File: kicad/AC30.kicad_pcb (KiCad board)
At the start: 2 copper layers, 173 x 97.5 mm, 84 parts, among them IC10 555, IC11 4001, IC12 1489, IC13 4070, IC14 4053, IC15 1488, IC6 4053, IC7 4049, IC8 4013, IC9 4023, J1 Front panel harness 1, J2 Front panel harness 2, J3 Computer interface (COMP), J4 Control interface, J5 Terminal interface (TERM), Q10 2N5087, Q11 2N5087, Q5 2N5210, Q6 2N5210, Q7 2N5210, Q8 2N5210, Q9 2N5087

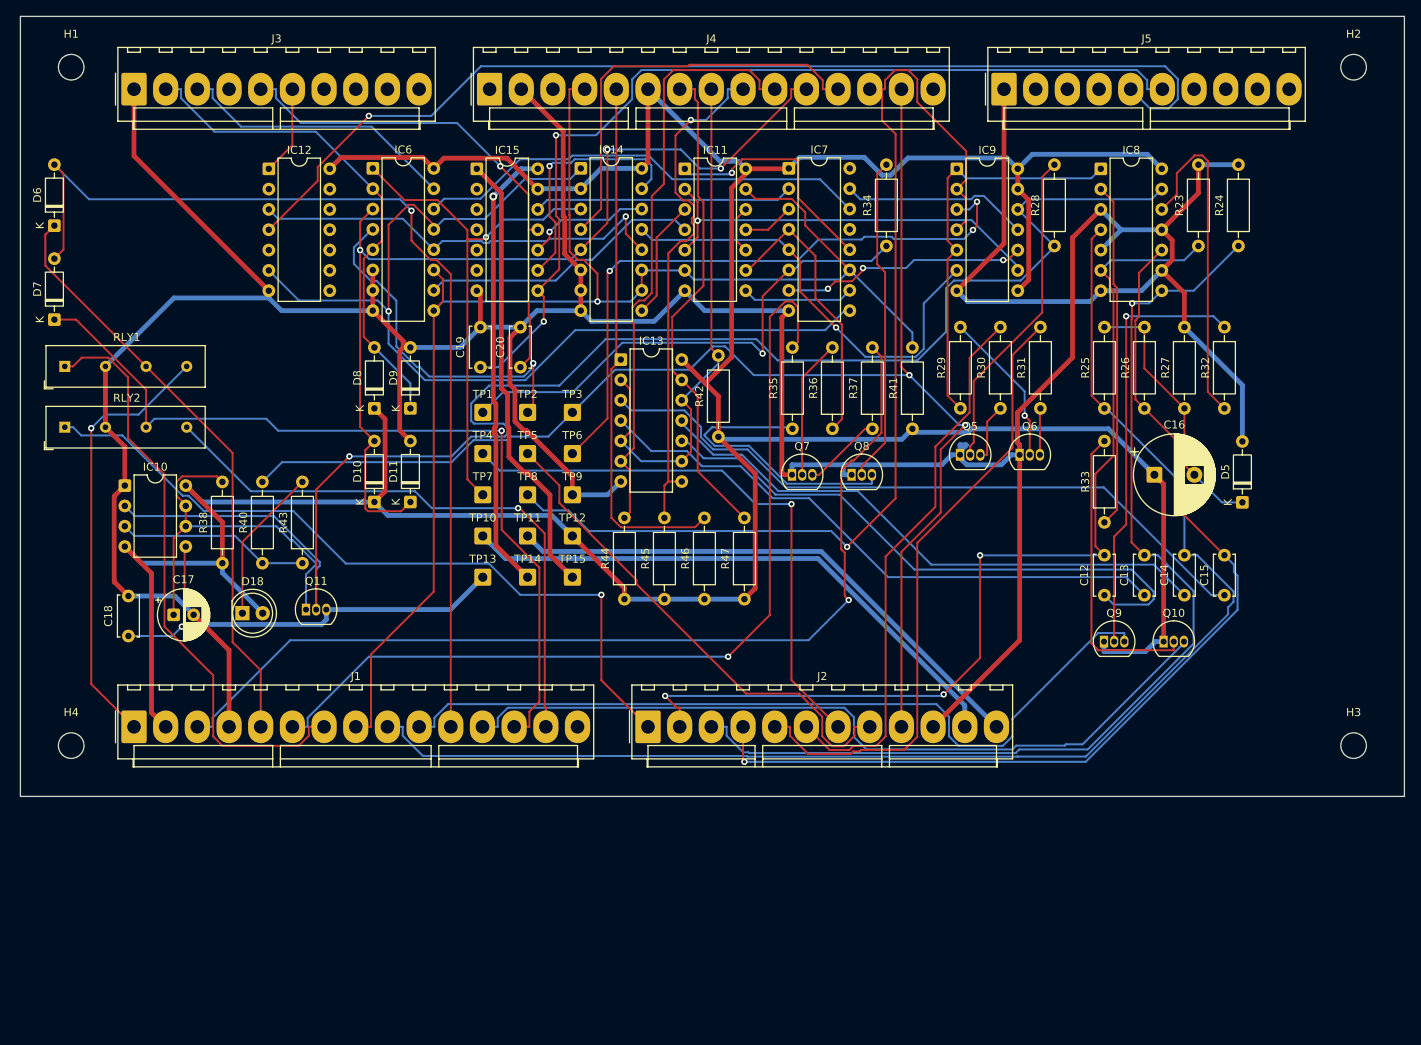
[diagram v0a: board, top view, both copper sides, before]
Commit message: Wire mod/demod and external power supply; retry routing until DRC-clean
- Transcribe docs/ac30_mod_demod.pdf onto sheet 2: modulator (IC5A/B,
  IC2A, IC4A filter) and demodulator (IC4B comparator, IC3C/D edge pulses,
  carrier detect, missing-pulse detector, R16 timer, IC1A data out, 16X
  clock out). The mod/demod interface solder pads are removed.
- Transcribe docs/ac30_PS.pdf onto new sheet 3 as an external unit (no
  footprints): line cord, S6, F1, T1, bridge D14-D17, +/-13 V, +/-7.5 V
  zener rails, 7805. IC16 GND taken as GND (drawing ties it to -13 V).
- Board gets through-hole power input pads TP1-TP6 (+5V, GND, +13V, -13V,
  +7.5V, -7.5V) with rail names on the silkscreen, plus C23-C25 +5 V
  bypass. IC4 on +/-7.5 V, IC15 on +/-13 V. J2 18 VAC pins now unused.
- Corner mounting holes H1-H4, 6.35 mm in from each edge (artwork).
- Placement weighs all nets except +5V/GND; build.sh routes the placed
  board afresh up to 4 times and keeps the first DRC-clean result.
- Board 173.0 x 121.5 mm, fully routed; ERC, DRC (all severities) and
  schematic parity clean. AC30-settings.md updated.

Co-Authored-By: Claude Opus 5.5 <noreply@anthropic.com>
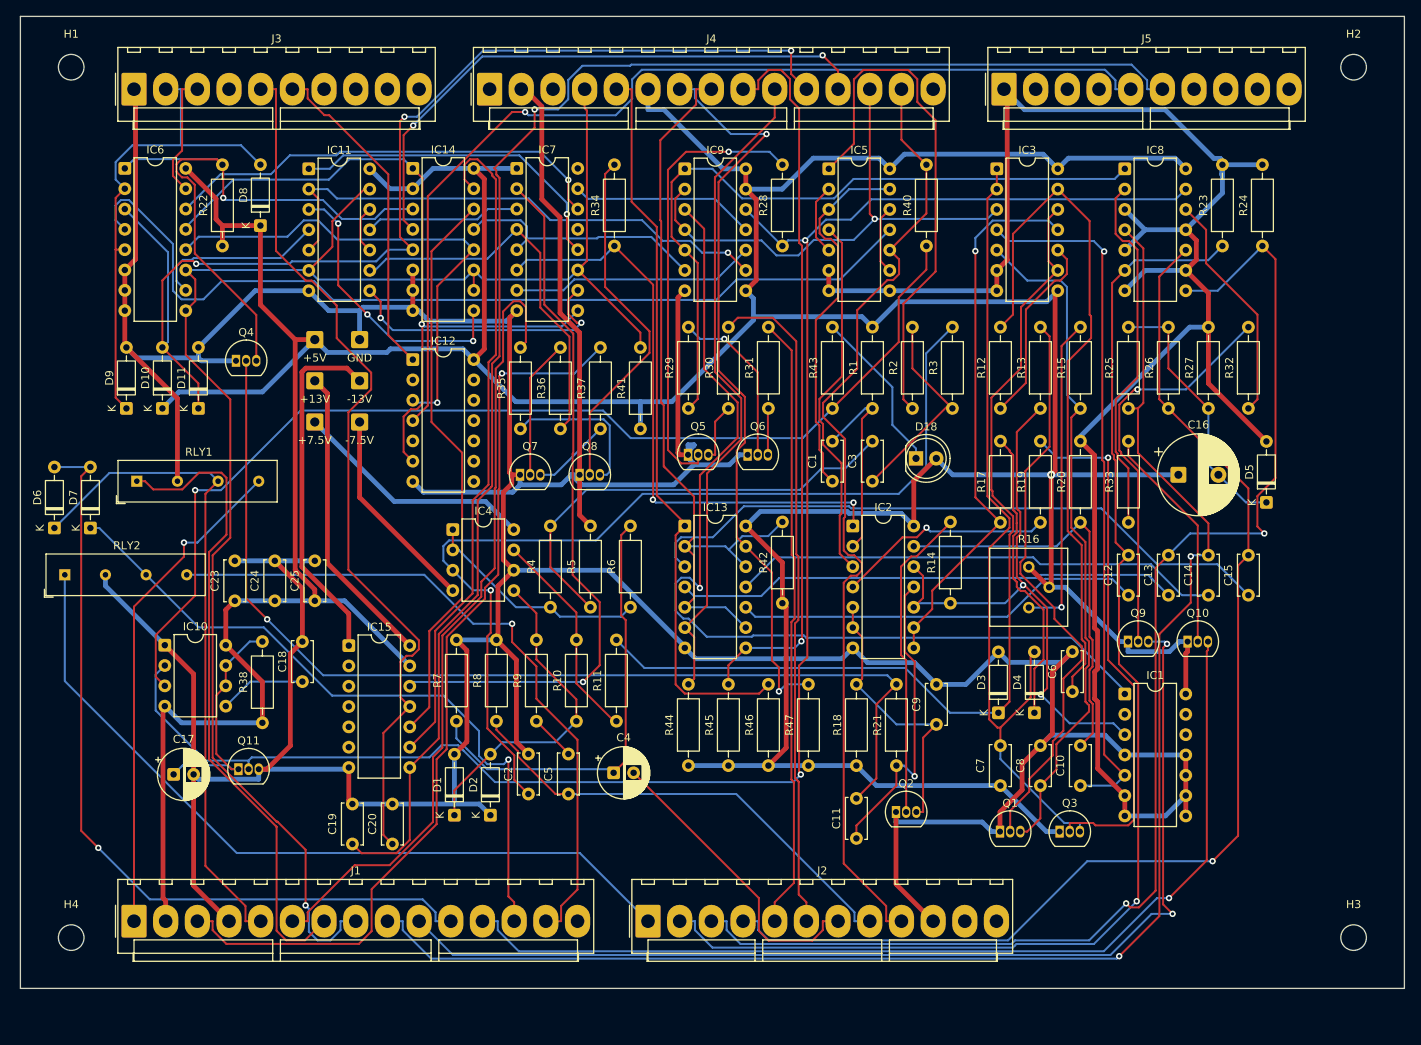
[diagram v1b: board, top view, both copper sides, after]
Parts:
- removed TP10: 18 VAC A (from J2 / T1), Connector_Wire:SolderWire-0.5sqmm_1x01_D0.9mm_OD2.1mm
- removed TP11: 18 VAC B (from J2 / T1), Connector_Wire:SolderWire-0.5sqmm_1x01_D0.9mm_OD2.1mm
- removed TP12: +5V (regulated), Connector_Wire:SolderWire-0.5sqmm_1x01_D0.9mm_OD2.1mm
- removed TP13: GND (power), Connector_Wire:SolderWire-0.5sqmm_1x01_D0.9mm_OD2.1mm
- removed TP14: RS-232 V+ (IC15 pin 14), Connector_Wire:SolderWire-0.5sqmm_1x01_D0.9mm_OD2.1mm
- removed TP15: RS-232 V- (IC15 pin 1), Connector_Wire:SolderWire-0.5sqmm_1x01_D0.9mm_OD2.1mm
- removed TP7: 16X CLOCK OUT (from demodulator), Connector_Wire:SolderWire-0.5sqmm_1x01_D0.9mm_OD2.1mm
- removed TP8: CARRIER DETECT (from demodulator), Connector_Wire:SolderWire-0.5sqmm_1x01_D0.9mm_OD2.1mm
- removed TP9: GND (mod/demod), Connector_Wire:SolderWire-0.5sqmm_1x01_D0.9mm_OD2.1mm
- added C1: 1000pF, Capacitor_THT:C_Disc_D5.0mm_W2.5mm_P5.00mm, F.Cu at (131.5, 87.6)
- added C10: 2700pF, Capacitor_THT:C_Disc_D5.0mm_W2.5mm_P5.00mm, F.Cu at (162.5, 125.7)
- added C11: 470pF, Capacitor_THT:C_Disc_D5.0mm_W2.5mm_P5.00mm, F.Cu at (134.5, 132.2)
- added C2: 2000pF, Capacitor_THT:C_Disc_D5.0mm_W2.5mm_P5.00mm, F.Cu at (93.5, 126.7)
- added C23: 0.1uF, Capacitor_THT:C_Disc_D5.0mm_W2.5mm_P5.00mm, F.Cu at (56.8, 102.5)
- added C24: 0.1uF, Capacitor_THT:C_Disc_D5.0mm_W2.5mm_P5.00mm, F.Cu at (61.8, 102.5)
- added C25: 0.1uF, Capacitor_THT:C_Disc_D5.0mm_W2.5mm_P5.00mm, F.Cu at (66.8, 102.5)
- added C3: 0.022uF, Capacitor_THT:C_Disc_D5.0mm_W2.5mm_P5.00mm, F.Cu at (136.5, 87.6)
- added C4: 1uF 15V, Capacitor_THT:CP_Radial_D6.3mm_P2.50mm, F.Cu at (104.2, 124.0)
- added C5: 0.01uF, Capacitor_THT:C_Disc_D5.0mm_W2.5mm_P5.00mm, F.Cu at (98.5, 126.7)
- added C6: 1000pF, Capacitor_THT:C_Disc_D5.0mm_W2.5mm_P5.00mm, F.Cu at (161.5, 113.9)
- added C7: 0.047uF, Capacitor_THT:C_Disc_D5.0mm_W2.5mm_P5.00mm, F.Cu at (152.5, 125.7)
- added C8: 0.022uF, Capacitor_THT:C_Disc_D5.0mm_W2.5mm_P5.00mm, F.Cu at (157.5, 125.7)
- added C9: 0.047uF, Capacitor_THT:C_Disc_D5.0mm_W2.5mm_P5.00mm, F.Cu at (144.5, 118.0)
- added D1: 1N4148, Diode_THT:D_DO-35_SOD27_P7.62mm_Horizontal, F.Cu at (84.2, 129.3)
- added D2: 1N4148, Diode_THT:D_DO-35_SOD27_P7.62mm_Horizontal, F.Cu at (88.8, 129.3)
- added D3: 1N4732 4.7V, Diode_THT:D_DO-35_SOD27_P7.62mm_Horizontal, F.Cu at (152.2, 116.5)
- added D4: 1N4148, Diode_THT:D_DO-35_SOD27_P7.62mm_Horizontal, F.Cu at (156.8, 116.5)
- added IC1: 4013, Package_DIP:DIP-14_W7.62mm, F.Cu at (168.1, 114.2)
- added IC2: 4001, Package_DIP:DIP-14_W7.62mm, F.Cu at (134.1, 93.2)
- added IC3: 4070, Package_DIP:DIP-14_W7.62mm, F.Cu at (152.1, 48.5)
- added IC4: 4558, Package_DIP:DIP-8_W7.62mm, F.Cu at (84.0, 93.7)
- added IC5: 4013, Package_DIP:DIP-14_W7.62mm, F.Cu at (131.1, 48.5)
- added Q1: 2N5210, Package_TO_SOT_THT:TO-92_Inline, F.Cu at (152.4, 131.4)
- added Q2: 2N5210, Package_TO_SOT_THT:TO-92_Inline, F.Cu at (139.4, 128.9)
- added Q3: 2N5087, Package_TO_SOT_THT:TO-92_Inline, F.Cu at (159.9, 131.4)
- added Q4: 2N5210, Package_TO_SOT_THT:TO-92_Inline, F.Cu at (57.0, 72.5)
- added R1: 33K, Resistor_THT:R_Axial_DIN0207_L6.3mm_D2.5mm_P10.16mm_Horizontal, F.Cu at (136.5, 78.5)
- added R10: 330K, Resistor_THT:R_Axial_DIN0207_L6.3mm_D2.5mm_P10.16mm_Horizontal, F.Cu at (99.5, 117.6)
- added R11: 10K, Resistor_THT:R_Axial_DIN0207_L6.3mm_D2.5mm_P10.16mm_Horizontal, F.Cu at (104.5, 117.6)
- added R12: 10K, Resistor_THT:R_Axial_DIN0207_L6.3mm_D2.5mm_P10.16mm_Horizontal, F.Cu at (152.5, 78.5)
- added R13: 22K, Resistor_THT:R_Axial_DIN0207_L6.3mm_D2.5mm_P10.16mm_Horizontal, F.Cu at (157.5, 78.5)
- added R14: 22K, Resistor_THT:R_Axial_DIN0207_L6.3mm_D2.5mm_P10.16mm_Horizontal, F.Cu at (146.2, 102.8)
- added R15: 10K, Resistor_THT:R_Axial_DIN0207_L6.3mm_D2.5mm_P10.16mm_Horizontal, F.Cu at (162.5, 78.5)
- added R16: 20K trim, Potentiometer_THT:Potentiometer_Bourns_3386P_Vertical, F.Cu at (156.1, 103.4)
- added R17: 100K, Resistor_THT:R_Axial_DIN0207_L6.3mm_D2.5mm_P10.16mm_Horizontal, F.Cu at (152.5, 92.8)
- added R18: 100K, Resistor_THT:R_Axial_DIN0207_L6.3mm_D2.5mm_P10.16mm_Horizontal, F.Cu at (134.5, 123.2)
- added R19: 10K, Resistor_THT:R_Axial_DIN0207_L6.3mm_D2.5mm_P10.16mm_Horizontal, F.Cu at (157.5, 92.8)
- added R2: 10K, Resistor_THT:R_Axial_DIN0207_L6.3mm_D2.5mm_P10.16mm_Horizontal, F.Cu at (141.5, 78.5)
- added R20: 10K, Resistor_THT:R_Axial_DIN0207_L6.3mm_D2.5mm_P10.16mm_Horizontal, F.Cu at (162.5, 92.8)
- added R21: 10K, Resistor_THT:R_Axial_DIN0207_L6.3mm_D2.5mm_P10.16mm_Horizontal, F.Cu at (139.5, 123.2)
- added R22: 10K, Resistor_THT:R_Axial_DIN0207_L6.3mm_D2.5mm_P10.16mm_Horizontal, F.Cu at (55.2, 58.2)
- added R3: 10K, Resistor_THT:R_Axial_DIN0207_L6.3mm_D2.5mm_P10.16mm_Horizontal, F.Cu at (146.5, 78.5)
- added R4: 330, Resistor_THT:R_Axial_DIN0207_L6.3mm_D2.5mm_P10.16mm_Horizontal, F.Cu at (96.2, 103.3)
- added R5: 2.2K, Resistor_THT:R_Axial_DIN0207_L6.3mm_D2.5mm_P10.16mm_Horizontal, F.Cu at (101.2, 103.3)
- added R6: 4.7K, Resistor_THT:R_Axial_DIN0207_L6.3mm_D2.5mm_P10.16mm_Horizontal, F.Cu at (106.2, 103.3)
- added R7: 470, Resistor_THT:R_Axial_DIN0207_L6.3mm_D2.5mm_P10.16mm_Horizontal, F.Cu at (84.5, 117.6)
- added R8: 100K, Resistor_THT:R_Axial_DIN0207_L6.3mm_D2.5mm_P10.16mm_Horizontal, F.Cu at (89.5, 117.6)
- added R9: 10K, Resistor_THT:R_Axial_DIN0207_L6.3mm_D2.5mm_P10.16mm_Horizontal, F.Cu at (94.5, 117.6)
- TP1: value DATA IN (to modulator) -> +5V
- TP2: value 16X CLOCK IN (to modulator) -> GND
- TP3: value ~{CARRIER ENABLE} (to modulator) -> +13V
- TP4: value AUDIO OUT (from modulator) -> -13V
- TP5: value AUDIO IN (to demodulator) -> +7.5V
- TP6: value DATA OUT (from demodulator) -> -7.5V
- moved R40 92.0 mm to (143.2, 58.2)
- moved D18 86.4 mm to (141.9, 84.8)
- moved R43 69.0 mm to (131.5, 78.5)
- moved C19 61.7 mm to (71.5, 132.9)
- moved C20 61.7 mm to (76.5, 132.9)
- moved IC15 61.7 mm to (71.0, 108.2)
- moved IC11 47.0 mm to (66.0, 48.5)
- moved D6 37.8 mm to (34.2, 93.5)
- moved D9 35.5 mm to (43.2, 78.5)
- moved IC9 34.0 mm to (113.0, 48.5)
- moved IC7 34.0 mm to (92.0, 48.5)
- moved Q6 34.0 mm to (120.9, 84.3)
- moved Q7 34.0 mm to (92.5, 86.8)
- moved Q8 34.0 mm to (99.9, 86.8)
- moved R28 34.0 mm to (125.2, 58.2)
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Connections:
- IC15 pad 1: V_RS232- -> -13V
- IC15 pad 14: V_RS232+ -> +13V
- J2 pad 11: 18VAC_A -> unconnected-(J2-Pin_11-Pad11)
- J2 pad 12: 18VAC_B -> unconnected-(J2-Pin_12-Pad12)
- TP1 pad 1: DATA_IN -> +5V
- TP2 pad 1: CLOCK_IN -> GND
- TP3 pad 1: CARRIER_EN_N -> +13V
- TP4 pad 1: AUDIO_OUT -> -13V
- TP5 pad 1: AUDIO_IN -> +7.5V
- TP6 pad 1: DATA_OUT -> -7.5V
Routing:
- net GND: track 557.8 -> 869.7 mm
- net +5V: track 441.4 -> 639.8 mm, vias 0 -> 1
- net /Mod/Demod & power input/DEM_Q4B: track 0.00 -> 131.8 mm, vias 0 -> 1
- net /Mod/Demod & power input/DEM_LIM: track 0.00 -> 120.7 mm
- net /Mod/Demod & power input/MOD_F2: track 0.00 -> 120.3 mm, vias 0 -> 1
- net /DELAY_OUT: track 24.1 -> 138.9 mm, vias 0 -> 1
- net /Mod/Demod & power input/DEM_CD: track 0.00 -> 102.8 mm
- net /Mod/Demod & power input/DEM_DLY: track 0.00 -> 87.6 mm
- net /Mod/Demod & power input/DEM_BIT: track 0.00 -> 87.4 mm, vias 0 -> 1
- net /Mod/Demod & power input/DEM_TIMER: track 0.00 -> 85.3 mm
- net /TERM_RS232_IN: track 117.4 -> 190.8 mm, vias 2 -> 1
- net /Mod/Demod & power input/DEM_PULSE: track 0.00 -> 72.8 mm, vias 0 -> 2
- net /Mod/Demod & power input/DEM_Q1B: track 0.00 -> 71.9 mm
- net 18VAC_A: track 71.7 -> 0.00 mm
- net CLOCK_IN: track 44.6 -> 114.6 mm, vias 1 -> 0
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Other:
- board size 173 x 97.5 mm -> 173 x 121.5 mm

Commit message: Replace power input pads with J12, a 6-pin KK-396 header on the bottom edge
- J12 (Molex KK-396 A-41791-0006) replaces solder pads TP1-TP6 for the
  external supply: 1 GND, 2 +5V, 3 +13V, 4 -13V, 5 +7.5V, 6 -7.5V.
  Placed in the bottom connector row next to J2, clear of the corner hole.
- build.sh: if no routing attempt is DRC-clean, up to 3 finishing passes
  route only what is left on the best result, each checked by DRC.
- Board 173.5 x 122.0 mm, fully routed; ERC, DRC (all severities) and
  schematic parity clean. AC30-settings.md updated (power input, drill
  table, routing, positions).

Co-Authored-By: Claude Opus 5.5 <noreply@anthropic.com>
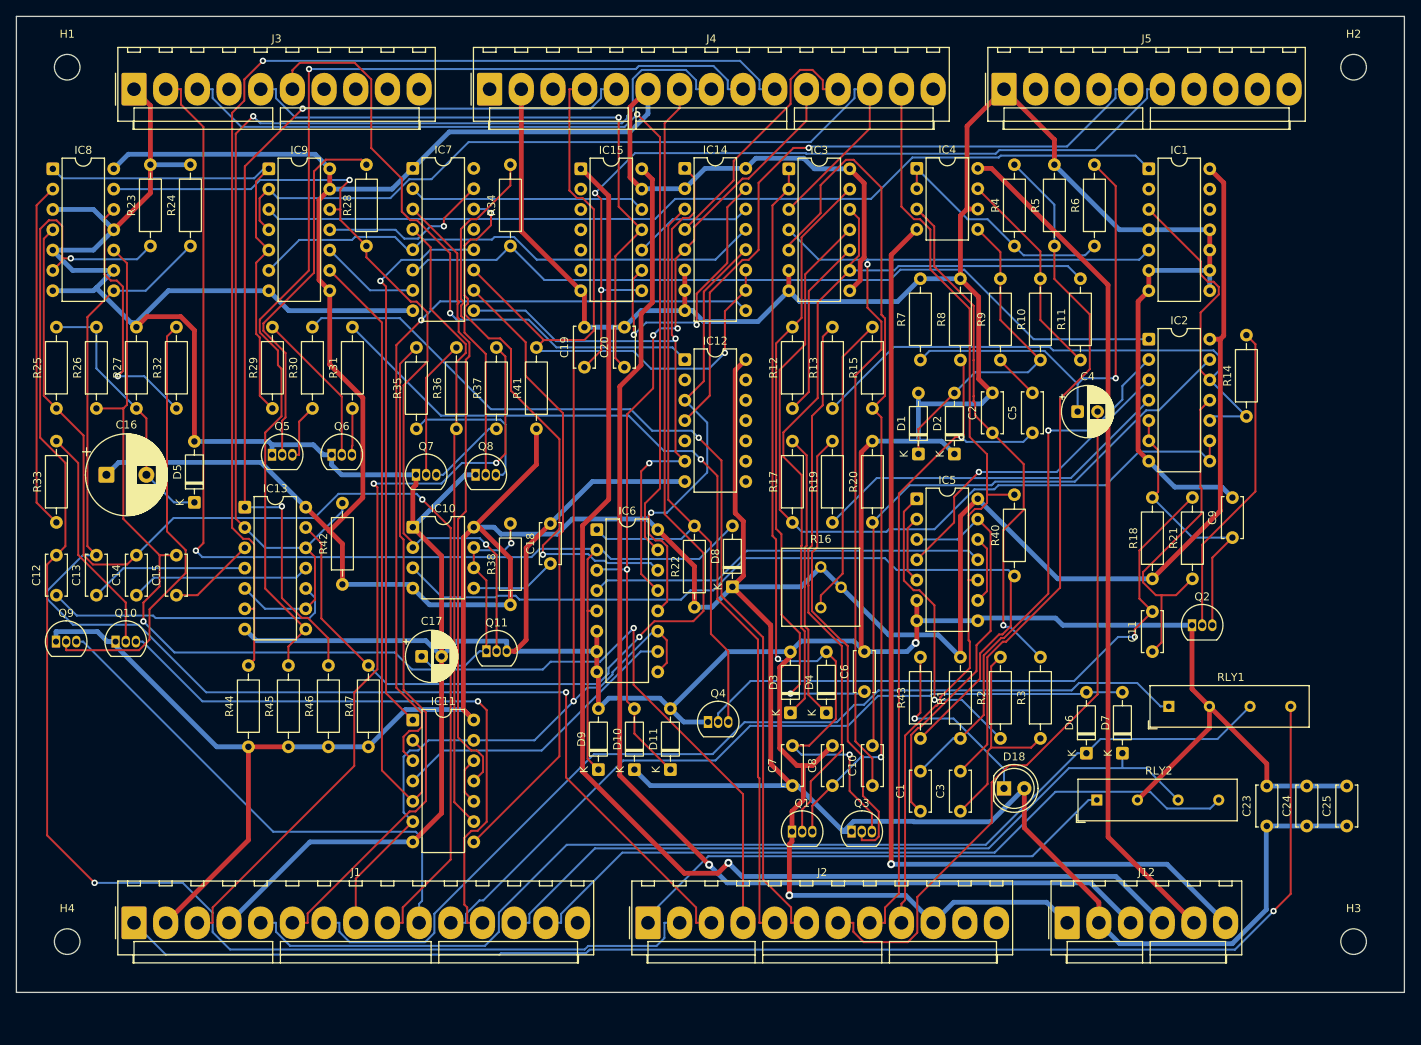
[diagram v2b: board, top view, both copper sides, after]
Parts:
- removed TP1: +5V, Connector_Wire:SolderWire-0.5sqmm_1x01_D0.9mm_OD2.1mm
- removed TP2: GND, Connector_Wire:SolderWire-0.5sqmm_1x01_D0.9mm_OD2.1mm
- removed TP3: +13V, Connector_Wire:SolderWire-0.5sqmm_1x01_D0.9mm_OD2.1mm
- removed TP4: -13V, Connector_Wire:SolderWire-0.5sqmm_1x01_D0.9mm_OD2.1mm
- removed TP5: +7.5V, Connector_Wire:SolderWire-0.5sqmm_1x01_D0.9mm_OD2.1mm
- removed TP6: -7.5V, Connector_Wire:SolderWire-0.5sqmm_1x01_D0.9mm_OD2.1mm
- added J12: Power input, Connector_Molex:Molex_KK-396_A-41791-0006_1x06_P3.96mm_Vertical, F.Cu at (160.8, 142.8)
- moved C12 134.0 mm to (34.5, 101.8)
- moved C13 134.0 mm to (39.5, 101.8)
- moved C14 134.0 mm to (44.5, 101.8)
- moved C15 134.0 mm to (49.5, 101.8)
- moved C16 134.0 mm to (40.8, 86.8)
- moved D5 134.0 mm to (51.8, 90.2)
- moved IC8 134.0 mm to (34.0, 48.5)
- moved Q10 134.0 mm to (41.9, 107.7)
- moved Q9 134.0 mm to (34.5, 107.7)
- moved R23 134.0 mm to (46.2, 58.2)
- moved R24 134.0 mm to (51.2, 58.2)
- moved R25 134.0 mm to (34.5, 78.5)
- moved R26 134.0 mm to (39.5, 78.5)
- moved R27 134.0 mm to (44.5, 78.5)
- moved R32 134.0 mm to (49.5, 78.5)
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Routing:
- net -13V: track 44.7 -> 159.6 mm, vias 0 -> 1
- net /REC_EN: track 220.7 -> 108.2 mm
- net +13V: track 38.0 -> 149.5 mm, vias 0 -> 1
- net /MOTOR_1A: track 62.4 -> 172.8 mm
- net +5V: track 639.8 -> 744.9 mm, vias 1 -> 0
- net /CPU_CLK_IN: track 15.5 -> 115.3 mm, vias 0 -> 1
- net -7.5V: track 25.9 -> 125.5 mm, vias 0 -> 1
- net /CPU_CLK_OUT: track 62.3 -> 160.9 mm, vias 0 -> 1
- net /TERM_RS232_IN: track 190.8 -> 105.1 mm, vias 1 -> 2
- net +7.5V: track 30.4 -> 106.5 mm
- net /REC_RLY_DRV: track 135.0 -> 64.1 mm, vias 2 -> 0
- net /STOP_REC_P: track 81.6 -> 11.0 mm
- net /SEL_TERM_CLK: track 35.7 -> 101.7 mm, vias 3 -> 1
- net CLOCK_IN: track 114.6 -> 50.2 mm
- net /START_RECORD: track 82.6 -> 146.3 mm, vias 0 -> 1
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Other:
- board size 173 x 121.5 mm -> 173.5 x 122 mm
